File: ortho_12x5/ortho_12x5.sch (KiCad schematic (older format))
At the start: 1 part, among them SW1 SW_SPST

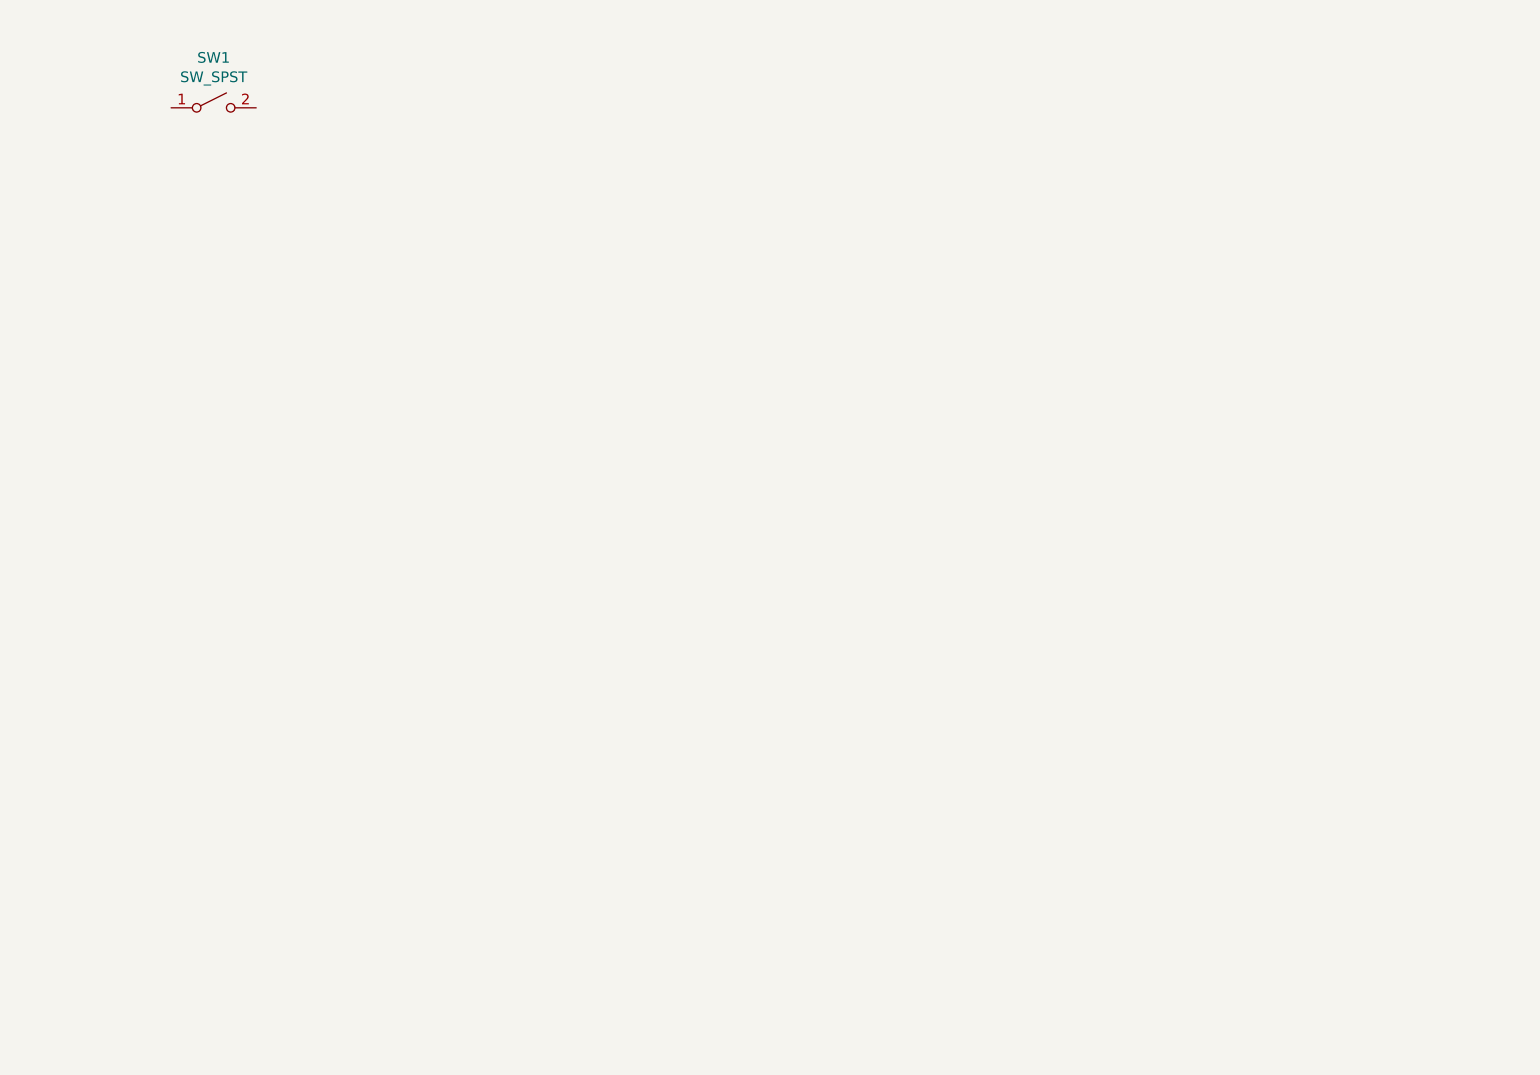
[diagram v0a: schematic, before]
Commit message: Add main grid to schematic
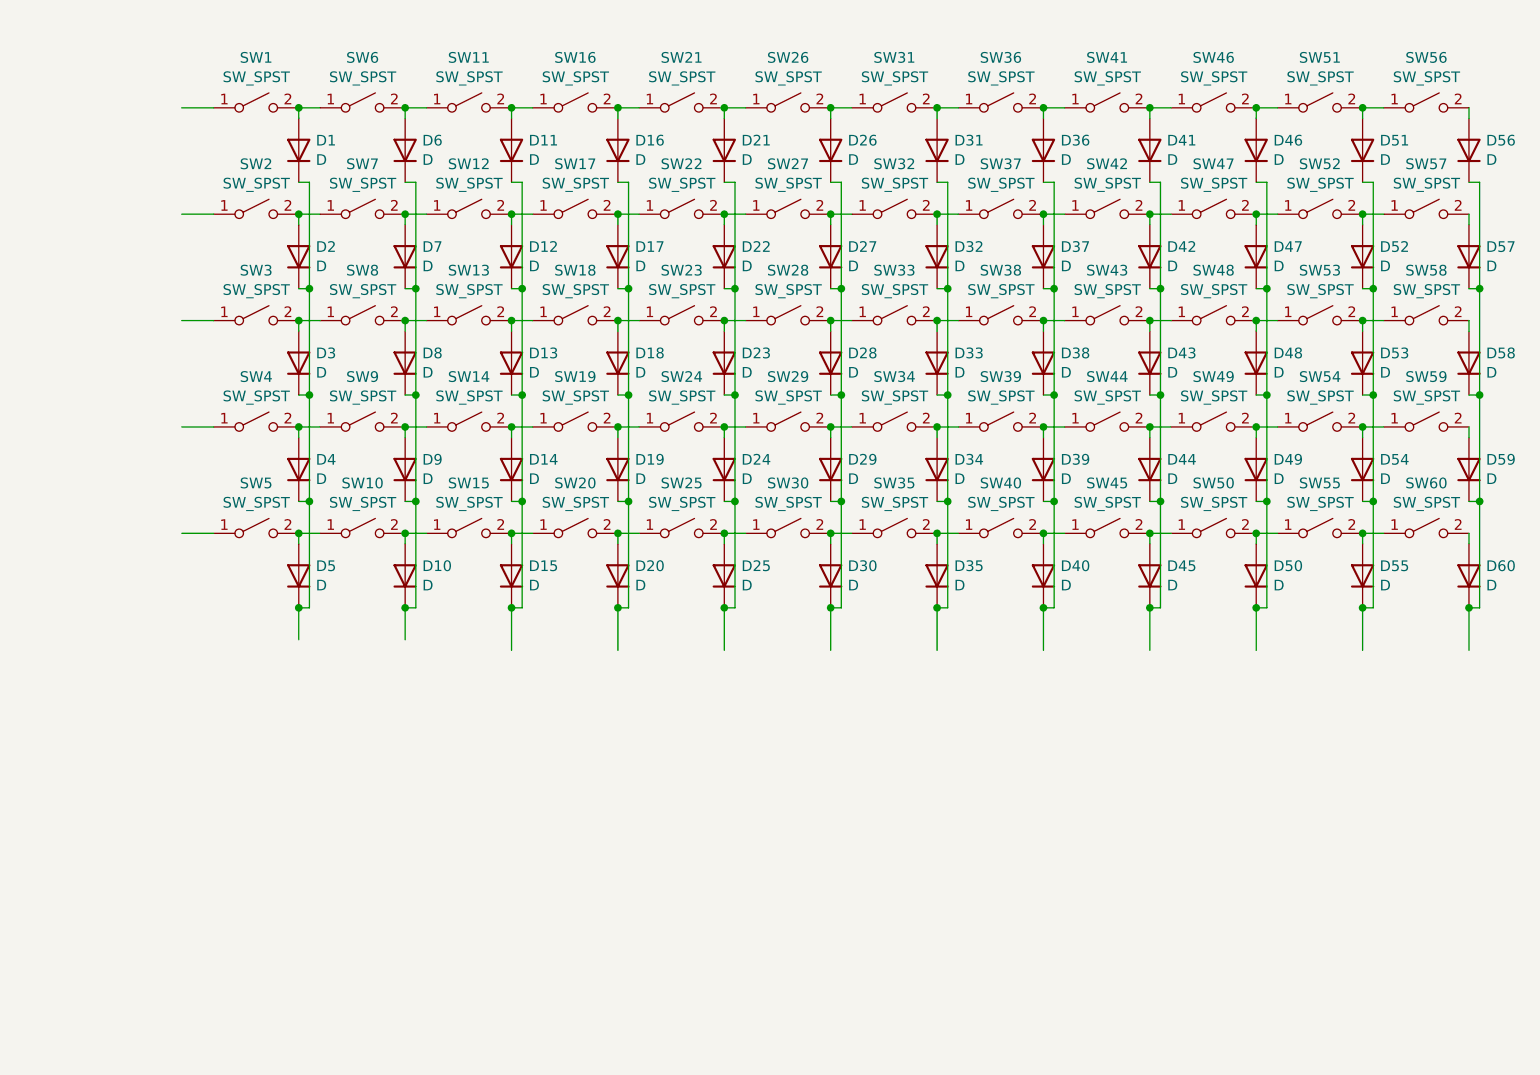
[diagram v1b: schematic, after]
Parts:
- added D1, D10, D11, D12, D13, D14, D15, D16, D17, D18, D19, D2, D20, D21, D22, D23, D24, D25, D26, D27, D28, D29, D3, D30, D31, D32, D33, D34, D35, D36, D37, D38, D39, D4, D40, D41, D42, D43, D44, D45, D46, D47, D48, D49, D5, D50, D51, D52, D53, D54, D55, D56, D57, D58, D59, D6, D60, D7, D8, D9: D, symbol Device:D
- added SW10, SW11, SW12, SW13, SW14, SW15, SW16, SW17, SW18, SW19, SW2, SW20, SW21, SW22, SW23, SW24, SW25, SW26, SW27, SW28, SW29, SW3, SW30, SW31, SW32, SW33, SW34, SW35, SW36, SW37, SW38, SW39, SW4, SW40, SW41, SW42, SW43, SW44, SW45, SW46, SW47, SW48, SW49, SW5, SW50, SW51, SW52, SW53, SW54, SW55, SW56, SW57, SW58, SW59, SW6, SW60, SW7, SW8, SW9: SW_SPST, Button_Switch_Keyboard:SW_Cherry_MX_1.00u_PCB, symbol Switch:SW_SPST
- SW1: footprint (none) -> Button_Switch_Keyboard:SW_Cherry_MX_1.00u_PCB
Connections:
- wire segments 0 -> 240
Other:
- moved on the sheet: SW1

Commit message: Start layout
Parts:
- D1, D10, D11, D12, D13, D14, D15, D16, D17, D18, D19, D2, D20, D21, D22, D23, D24, D25, D26, D27, D28, D29, D3, D30, D31, D32, D33, D34, D35, D36, D37, D38, D39, D4, D40, D41, D42, D43, D44, D45, D46, D47, D48, D49, D5, D50, D51, D52, D53, D54, D55, D56, D57, D58, D59, D6, D60, D7, D8, D9: footprint (none) -> Diode_THT:D_DO-34_SOD68_P7.62mm_Horizontal

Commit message: Redo schematic
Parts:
- added J1: Conn_01x05, Connector_PinSocket_2.54mm:PinSocket_1x05_P2.54mm_Horizontal, symbol Connector_Generic:Conn_01x05
- added J2: Conn_01x12, Connector_PinHeader_2.54mm:PinHeader_1x12_P2.54mm_Horizontal, symbol Connector_Generic:Conn_01x12
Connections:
- wire segments 240 -> 270

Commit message: Fix schematic, place components; need route
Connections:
- net at J1.1 (Pin_1), SW1.1 (A), SW11.1 (A)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: now also SW41.1 (A)
- net at J1.2 (Pin_2), SW12.1 (A), SW17.1 (A)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: now also SW42.1 (A)
- net at J1.3 (Pin_3), SW13.1 (A), SW18.1 (A)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: now also SW43.1 (A)
- net at J1.4 (Pin_4), SW14.1 (A), SW19.1 (A)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: now also SW44.1 (A)
- net at J1.5 (Pin_5), SW10.1 (A), SW15.1 (A)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: now also SW45.1 (A)
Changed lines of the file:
@@
 	0    -1   -1   0
 $EndComp
-Wire Wire Line
-	5500 1450 5500 1500
 $Comp
 L Switch:SW_SPST SW41
@@
 	0    -1   -1   0
 $EndComp
-Wire Wire Line
-	5500 2000 5500 2050
 $Comp
 L Switch:SW_SPST SW42
@@
 	0    -1   -1   0
 $EndComp
-Wire Wire Line
-	5500 2550 5500 2600
 $Comp
 L Switch:SW_SPST SW43
@@
 	0    -1   -1   0
 $EndComp
-Wire Wire Line
-	5500 3100 5500 3150
 $Comp
 L Switch:SW_SPST SW44
@@
 	0    -1   -1   0
 $EndComp
-Wire Wire Line
-	5500 3650 5500 3700
 $Comp
 L Switch:SW_SPST SW45
@@
 Wire Wire Line
 	7450 4050 7450 5300
+Wire Wire Line
+	5500 1450 5500 1550
+Wire Wire Line
+	5500 3100 5500 3200
+Wire Wire Line
+	5500 3650 5500 3750
+Wire Wire Line
+	5500 2550 5500 2650
+Wire Wire Line
+	5500 2000 5500 2100
 $EndSCHEMATC
